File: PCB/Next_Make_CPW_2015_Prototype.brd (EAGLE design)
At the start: 41.9 x 36.8 mm, 6 parts

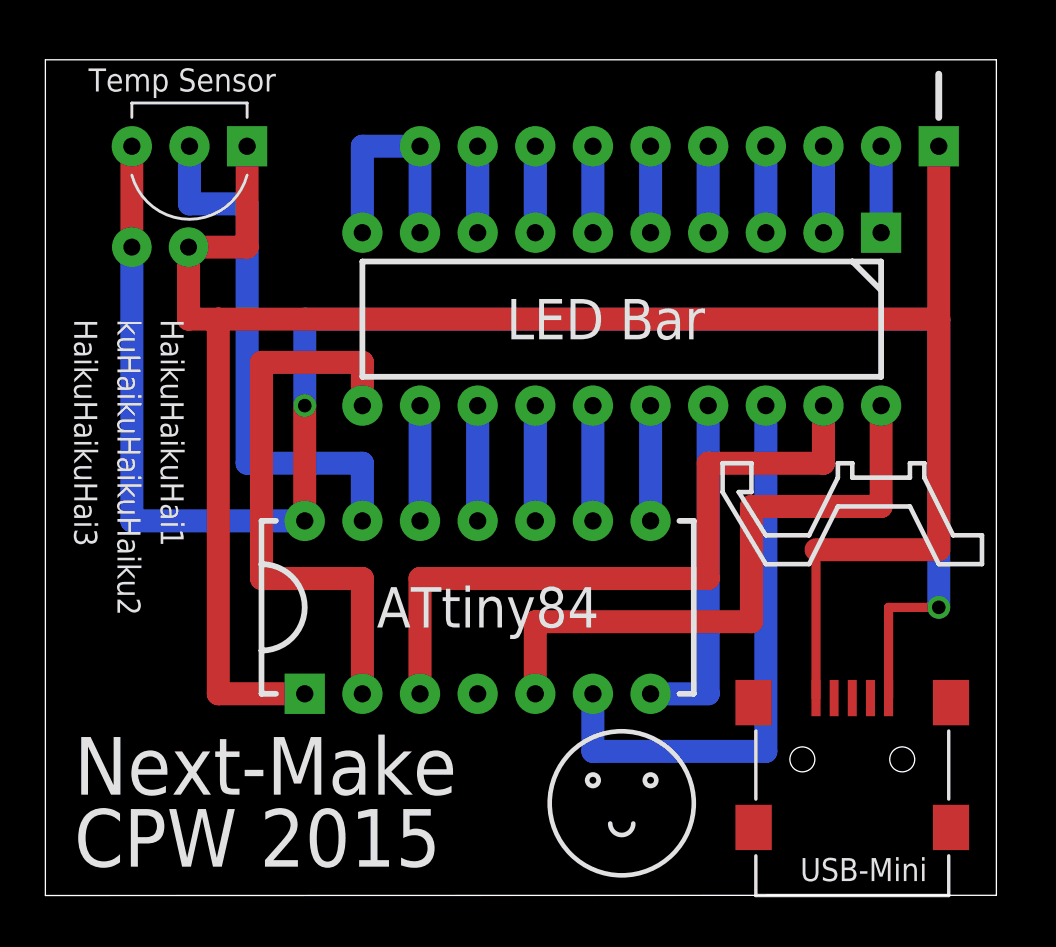
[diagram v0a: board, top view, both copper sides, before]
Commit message: updated board design with instuctions and resistive divider
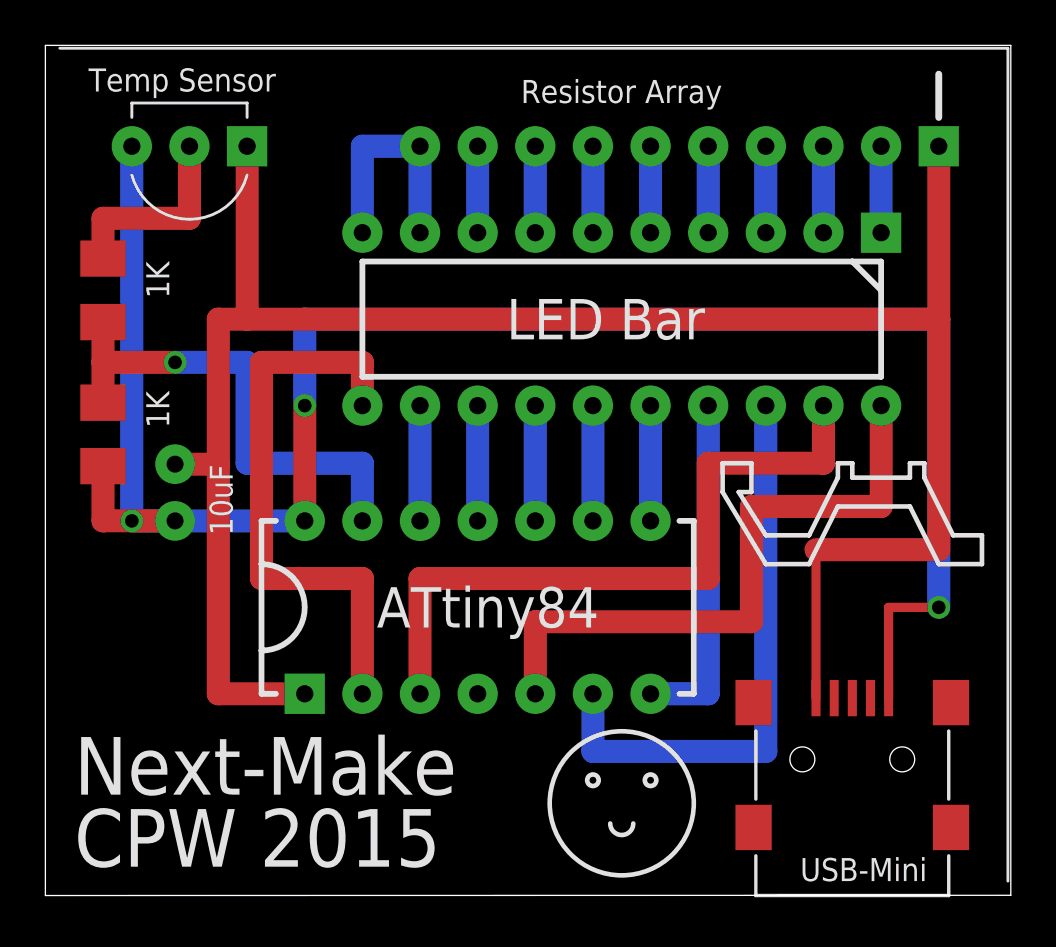
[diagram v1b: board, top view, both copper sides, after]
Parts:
- added R1, R2: 1K, rcl:M1206
- moved U$2 12.2 mm to (5.71, 16.5), turned to 90 degrees
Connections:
- new net N$9: R2.1, U$5.PIN_2
- net GND: now also R1.2
- net N$10: now also R1.1, R2.2; no longer U$5.PIN_2
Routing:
- net N$9: track 0.00 -> 8.76 mm
- net GND: track 79.9 -> 85.5 mm, vias 2 -> 3
- net N$10: track 24.1 -> 22.0 mm, vias 0 -> 1
- net 5V: track 93.3 -> 91.3 mm
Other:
- board size 41.9 x 36.8 mm -> 42.5 x 37.5 mm
- board text added: "10uF"
- board text added: "Resistor Array"
- board text added: "This is a thermometer that reads out"
- board text added: "To read, convert binary output"
- board text added: "the temperature in binary."
- board text added: "to base 10, then divide by 10"
- board text added: "to get temperature in Celcius."
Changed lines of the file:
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@@
 <board>
 <plain>
-<wire x1="41.91" y1="36.83" x2="0" y2="36.83" width="0" layer="20"/>
-<wire x1="0" y1="36.83" x2="0" y2="0" width="0" layer="20"/>
-<wire x1="0" y1="0" x2="41.91" y2="0.01" width="0" layer="20"/>
-<wire x1="41.91" y1="0.01" x2="41.91" y2="36.83" width="0" layer="20"/>
+<wire x1="42.545" y1="37.465" x2="0" y2="37.465" width="0" layer="20"/>
+<wire x1="0" y1="37.465" x2="0" y2="0" width="0" layer="20"/>
+<wire x1="0" y1="0" x2="42.545" y2="0.01" width="0" layer="20"/>
+<wire x1="42.545" y1="0.01" x2="42.545" y2="37.465" width="0" layer="20"/>
 <text x="14.605" y="11.811" size="1.778" layer="21" font="vector">ATtiny84</text>
 <text x="20.32" y="24.511" size="1.778" layer="21" font="vector">LED Bar</text>
@@
 <text x="1.27" y="1.27" size="2.54" layer="21" font="vector">CPW 2015</text>
 <text x="1.905" y="35.433" size="1.016" layer="21" font="vector">Temp Sensor</text>
-<text x="5.08" y="25.4" size="1.016" layer="21" font="vector" rot="SR270">HaikuHaikuHai1</text>
-<text x="3.175" y="25.4" size="1.016" layer="21" font="vector" rot="SR270">kuHaikuHaikuHaiku2</text>
-<text x="1.27" y="25.4" size="1.016" layer="21" font="vector" rot="SR270">HaikuHaikuHai3</text>
+<text x="31.115" y="5.715" size="1.016" layer="22" font="vector" rot="SMR0">HaikuHaikuHai1</text>
+<text x="31.115" y="3.81" size="1.016" layer="22" font="vector" rot="SMR0">kuHaikuHaikuHaiku2</text>
+<text x="31.115" y="1.905" size="1.016" layer="22" font="vector" rot="SMR0">HaikuHaikuHai3</text>
 <wire x1="36.83" y1="27.94" x2="36.83" y2="26.67" width="0.254" layer="21"/>
 <wire x1="36.83" y1="26.67" x2="36.83" y2="22.86" width="0.254" layer="21"/>
@@
 <circle x="26.67" y="5.08" radius="0.254" width="0.2032" layer="21"/>
 <wire x1="25.908" y1="3.175" x2="24.892" y2="3.175" width="0.2032" layer="21" curve="-180"/>
+<wire x1="42.418" y1="0.635" x2="42.418" y2="37.338" width="0.127" layer="21"/>
+<wire x1="42.418" y1="37.338" x2="0.635" y2="37.338" width="0.127" layer="21"/>
+<text x="20.955" y="34.925" size="1.016" layer="25" font="vector">Resistor Array</text>
+<text x="8.255" y="15.875" size="1.016" layer="25" font="vector" rot="R90">10uF</text>
+<text x="39.37" y="25.4" size="1.016" layer="26" font="vector" rot="MR0">This is a thermometer that reads out </text>
+<text x="39.37" y="24.13" size="1.016" layer="26" font="vector" rot="MR0">the temperature in binary.</text>
+<text x="36.195" y="14.097" size="1.016" layer="26" font="vector" rot="MR0">To read, convert binary output</text>
+<text x="36.195" y="12.319" size="1.016" layer="26" font="vector" rot="MR0">to base 10, then divide by 10</text>
+<text x="36.195" y="10.541" size="1.016" layer="26" font="vector" rot="MR0">to get temperature in Celcius.</text>
 </plain>
 <attributes>
@@
 <elements>
 <element name="U$1" library="Next_Make_CPW_2015" package="SIP-10" value="9X_1K_BUSSED_R" x="39.37" y="33.02" rot="R270"/>
-<element name="U$2" library="Next_Make_CPW_2015" package="CAP_FK18" value="10UF_FK18" x="3.81" y="28.575"/>
+<element name="U$2" library="Next_Make_CPW_2015" package="CAP_FK18" value="10UF_FK18" x="5.715" y="16.51" rot="R90"/>
 <element name="U$3" library="Next_Make_CPW_2015" package="PDIP-14" value="ATTINY84A" x="26.67" y="8.89" rot="R90"/>
 <element name="U$4" library="Next_Make_CPW_2015" package="LED_X10_BAR" value="LED_X10_BAR" x="36.83" y="29.21" rot="R270"/>
 <element name="U$5" library="Next_Make_CPW_2015" package="TO-92-3" value="MCP9701" x="8.89" y="33.02" rot="R180"/>
 <element name="U$6" library="Next_Make_CPW_2015" package="SMT_MINI_USB" value="USB_MINI" x="35.56" y="0" rot="R90"/>
+<element name="R1" library="rcl" package="M1206" value="1K" x="2.54" y="20.32" smashed="yes" rot="R270">
+<attribute name="VALUE" x="4.445" y="22.225" size="1.016" layer="21" font="vector" rot="R270"/>
+</element>
+<element name="R2" library="rcl" package="M1206" value="1K" x="2.54" y="26.67" smashed="yes" rot="R270">
+<attribute name="VALUE" x="4.445" y="27.94" size="1.016" layer="21" font="vector" rot="R270"/>
+</element>
 </elements>
 <signals>
@@
 <wire x1="39.37" y1="15.24" x2="39.37" y2="25.4" width="1.016" layer="1"/>
 <wire x1="39.37" y1="25.4" x2="39.37" y2="33.02" width="1.016" layer="1"/>
-<wire x1="8.89" y1="28.575" x2="8.89" y2="33.02" width="1.016" layer="1"/>
 <wire x1="11.43" y1="8.89" x2="7.62" y2="8.89" width="1.016" layer="1"/>
-<wire x1="7.62" y1="8.89" x2="7.62" y2="25.4" width="1.016" layer="1"/>
-<wire x1="7.62" y1="25.4" x2="39.37" y2="25.4" width="1.016" layer="1"/>
-<wire x1="8.89" y1="28.575" x2="6.31" y2="28.575" width="1.016" layer="1"/>
-<wire x1="7.62" y1="25.4" x2="6.31" y2="25.4" width="1.016" layer="1"/>
-<wire x1="6.31" y1="25.4" x2="6.31" y2="28.575" width="1.016" layer="1"/>
+<wire x1="7.62" y1="8.89" x2="7.62" y2="19.01" width="1.016" layer="1"/>
+<wire x1="7.62" y1="19.01" x2="7.62" y2="25.4" width="1.016" layer="1"/>
+<wire x1="7.62" y1="25.4" x2="8.89" y2="25.4" width="1.016" layer="1"/>
+<wire x1="8.89" y1="25.4" x2="39.37" y2="25.4" width="1.016" layer="1"/>
+<wire x1="5.715" y1="19.01" x2="7.62" y2="19.01" width="1.016" layer="1"/>
+<wire x1="8.89" y1="33.02" x2="8.89" y2="25.4" width="1.016" layer="1"/>
 </signal>
 <signal name="GND">
@@
 <wire x1="37.16" y1="8.7" x2="37.16" y2="12.7" width="0.4064" layer="1"/>
 <wire x1="37.16" y1="12.7" x2="39.37" y2="12.7" width="0.4064" layer="1"/>
-<via x="39.37" y="12.7" extent="1-16" drill="0.6" shape="square" alwaysstop="yes"/>
+<via x="39.37" y="12.7" extent="1-16" drill="0.6" shape="square"/>
 <wire x1="39.37" y1="12.7" x2="39.37" y2="25.4" width="1.016" layer="16"/>
 <wire x1="39.37" y1="25.4" x2="11.43" y2="25.4" width="1.016" layer="16"/>
 <wire x1="11.43" y1="25.4" x2="11.43" y2="21.59" width="1.016" layer="16"/>
-<via x="11.43" y="21.59" extent="1-16" drill="0.6" shape="square" alwaysstop="yes"/>
+<via x="11.43" y="21.59" extent="1-16" drill="0.6" shape="square"/>
 <wire x1="11.43" y1="21.59" x2="11.43" y2="16.51" width="1.016" layer="1"/>
-<wire x1="3.81" y1="33.02" x2="3.81" y2="28.575" width="1.016" layer="1"/>
-<wire x1="3.81" y1="28.575" x2="3.81" y2="16.51" width="1.016" layer="16"/>
-<wire x1="3.81" y1="16.51" x2="11.43" y2="16.51" width="1.016" layer="16"/>
+<wire x1="5.715" y1="16.51" x2="11.43" y2="16.51" width="1.016" layer="16"/>
+<contactref element="R1" pad="2"/>
+<wire x1="5.715" y1="16.51" x2="3.81" y2="16.51" width="1.016" layer="16"/>
+<wire x1="3.81" y1="16.51" x2="3.81" y2="33.02" width="1.016" layer="16"/>
+<via x="3.81" y="16.51" extent="1-16" drill="0.6" shape="square"/>
+<wire x1="3.81" y1="16.51" x2="2.54" y2="16.51" width="1.016" layer="1"/>
+<wire x1="2.54" y1="16.51" x2="2.54" y2="18.92" width="1.016" layer="1"/>
+<wire x1="3.81" y1="16.51" x2="5.715" y2="16.51" width="1.016" layer="1"/>
 </signal>
 <signal name="N$1">
@@
 <signal name="N$10">
 <contactref element="U$3" pad="PIN_13"/>
-<contactref element="U$5" pad="PIN_2"/>
 <wire x1="13.97" y1="16.51" x2="13.97" y2="19.05" width="1.016" layer="16"/>
 <wire x1="13.97" y1="19.05" x2="8.89" y2="19.05" width="1.016" layer="16"/>
-<wire x1="8.89" y1="19.05" x2="8.89" y2="30.48" width="1.016" layer="16"/>
-<wire x1="8.89" y1="30.48" x2="6.35" y2="30.48" width="1.016" layer="16"/>
-<wire x1="6.35" y1="30.48" x2="6.35" y2="33.02" width="1.016" layer="16"/>
+<contactref element="R2" pad="2"/>
+<contactref element="R1" pad="1"/>
+<wire x1="2.54" y1="21.72" x2="2.54" y2="23.495" width="1.016" layer="1"/>
+<wire x1="2.54" y1="23.495" x2="2.54" y2="25.27" width="1.016" layer="1"/>
+<wire x1="8.89" y1="19.05" x2="8.89" y2="23.495" width="1.016" layer="16"/>
+<wire x1="8.89" y1="23.495" x2="5.715" y2="23.495" width="1.016" layer="16"/>
+<via x="5.715" y="23.495" extent="1-16" drill="0.6" shape="square"/>
+<wire x1="5.715" y1="23.495" x2="2.54" y2="23.495" width="1.016" layer="1"/>
 </signal>
 <signal name="N$12">
@@
 <wire x1="13.97" y1="13.97" x2="13.97" y2="8.89" width="1.016" layer="1"/>
 </signal>
+<signal name="N$9">
+<contactref element="U$5" pad="PIN_2"/>
+<contactref element="R2" pad="1"/>
+<wire x1="6.35" y1="33.02" x2="6.35" y2="29.845" width="1.016" layer="1"/>
+<wire x1="6.35" y1="29.845" x2="2.54" y2="29.845" width="1.016" layer="1"/>
+<wire x1="2.54" y1="29.845" x2="2.54" y2="28.07" width="1.016" layer="1"/>
+</signal>
 </signals>
